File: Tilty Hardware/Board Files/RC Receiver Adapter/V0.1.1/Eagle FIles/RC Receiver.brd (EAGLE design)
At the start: 38.1 x 50.8 mm, 27 parts, among them U1 ATMEGA328P, U2 LM2931, U3 AP7313SOT23R, U4 C74HC407514-SOIC, Y1 16MHz

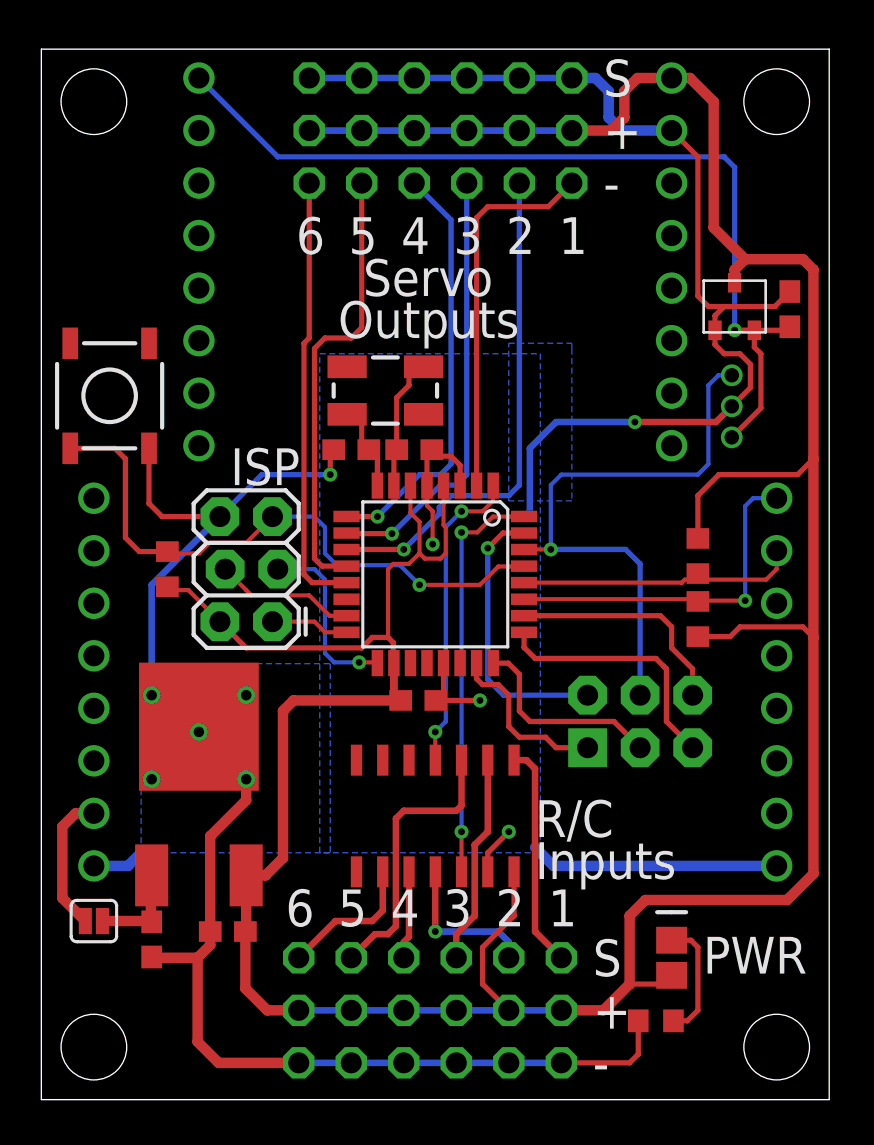
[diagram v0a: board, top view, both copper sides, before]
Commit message: R/C Receiver add-on work
fixed OR gate, moved reset button, corrected servo labels
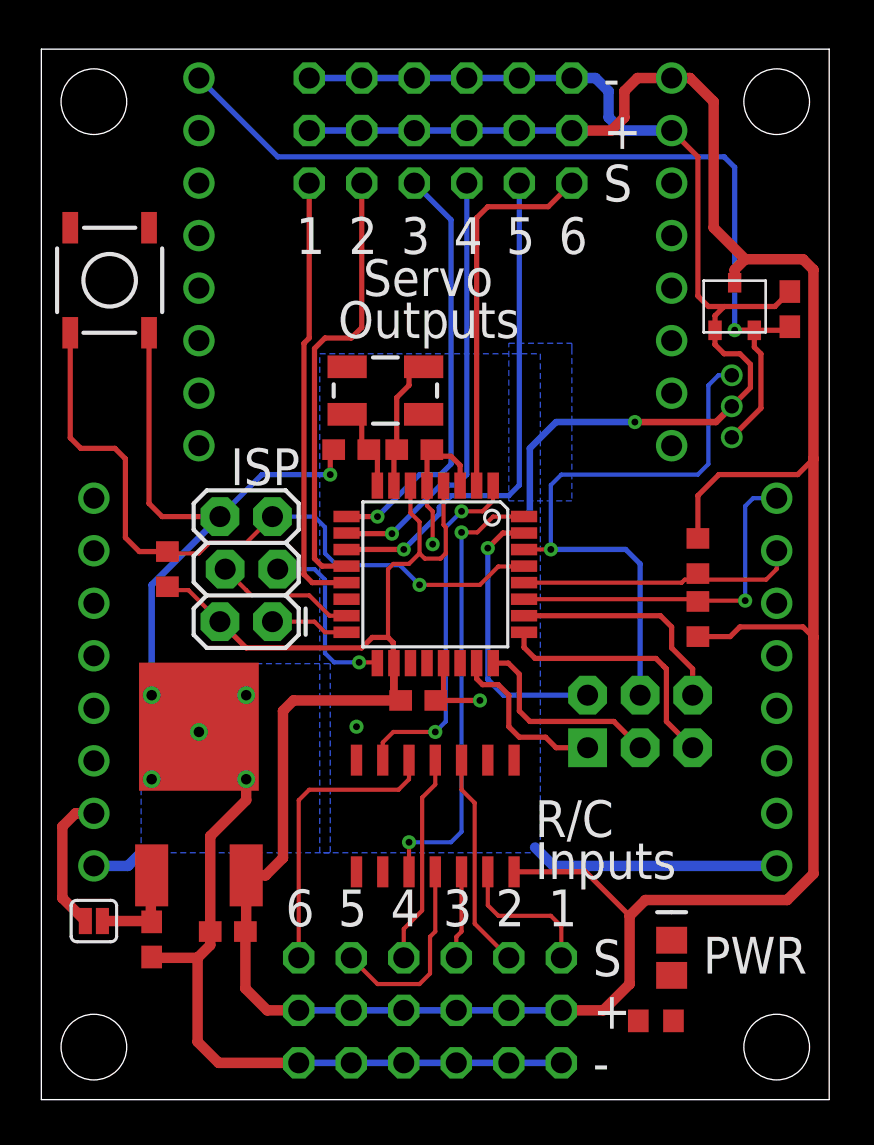
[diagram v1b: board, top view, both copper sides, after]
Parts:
- moved S1 5.59 mm to (3.30, 39.6)
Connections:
- net EVEN_CHAN: now also U1.1, U4.P$6; no longer U1.32, U4.P$12
- net GND: now also U4.P$7; no longer U4.P$13
- net ODD_CHAN: now also U1.32, U4.P$10; no longer U1.1, U4.P$4
- net SIGNAL_1: now also U4.P$13; no longer U4.P$1
- net SIGNAL_2: now also U4.P$3; no longer U4.P$11
- net SIGNAL_3: now also U4.P$12; no longer U4.P$2
- net SIGNAL_4: now also U4.P$4; no longer U4.P$10
- net SIGNAL_5: now also U4.P$11; no longer U4.P$3
- net SIGNAL_6: now also U4.P$5; no longer U4.P$9
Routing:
- net SIGNAL_6: track 6.88 -> 14.3 mm
- net ODD_CHAN: track 15.0 -> 22.0 mm
- net SIGNAL_4: track 4.26 -> 10.2 mm
- net SIGNAL_3: track 10.2 -> 4.26 mm
- net N$8: track 5.85 -> 0.00 mm
- net RESET: track 29.6 -> 34.9 mm
- net SIGNAL_5: track 13.6 -> 9.57 mm
- net SIGNAL_1: track 10.9 -> 7.12 mm
- net +5V: track 170.6 -> 167.0 mm
- net SIGNAL_2: track 7.42 -> 10.5 mm, vias 1 -> 0
- net EVEN_CHAN: track 19.8 -> 17.3 mm
- net GND: track 145.0 -> 142.7 mm

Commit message: RC Receiver add-on tweaking, updating things.todo handling
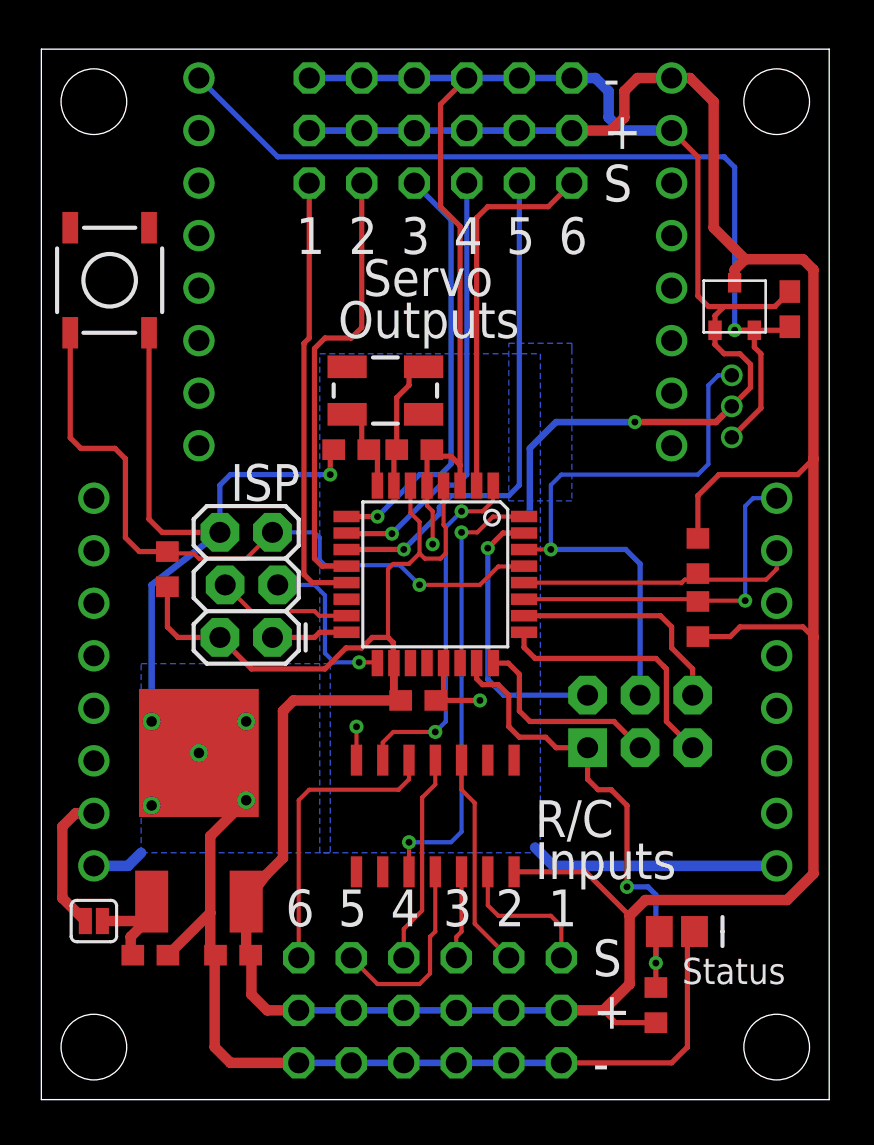
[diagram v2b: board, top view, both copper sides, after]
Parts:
- moved D1 1.30 mm to (30.7, 8.13), turned to 0 degrees
- moved U2 1.27 mm to (7.62, 14.0)
- moved C6 1.17 mm to (9.27, 6.99)
- moved C7 0.76 mm to (5.27, 6.99), turned to 0 degrees
- moved JP6 0.76 mm to (11.2, 22.4)
- moved R4 0.76 mm to (29.7, 4.57), turned to 270 degrees
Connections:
- removed net A0: JP10.1, U1.23
- removed net N$8: D1.2, R4.2
- new net STATUS_LED: D1.1, JP10.1, R4.1, U1.23
- net +5V: now also R4.2; no longer D1.1
- net GND: now also D1.2; no longer R4.1
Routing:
- net GND: track 142.7 -> 177.9 mm
- net STATUS_LED: track 0.00 -> 23.9 mm, vias 0 -> 2
- net A0: track 8.40 -> 0.00 mm
- net +5V: track 167.0 -> 171.3 mm
- net +24V: track 4.62 -> 7.75 mm
- net SCK: track 8.79 -> 8.02 mm
- net RESET: track 34.9 -> 34.3 mm
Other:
- board text added: "Status"
- board text removed: "PWR"

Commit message: Made final revisions to Tilty Omni and R/C Receiver adapter before ordering!
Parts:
- added D2: (no value), SparkFun-LED:LED-0805
- added R5: 220, resistor:R0603
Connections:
- new net N$4: D2.1, R5.1
- net +5V: now also R5.2
- net GND: now also D2.2
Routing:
- net +5V: track 171.3 -> 182.2 mm, vias 0 -> 1
- net N$4: track 0.00 -> 9.90 mm
- net GND: track 177.9 -> 178.4 mm
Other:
- board text added: "3v3"
- board text added: "5v"
- board text added: "GND"
- board text added: "ICSP"
- board text added: "PWR"
- board text added: "Reset"
- board text removed: "ISP"
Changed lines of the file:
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@@
 <setting verticaltext="up"/>
 </settings>
-<grid distance="0.01" unitdist="inch" unit="inch" style="lines" multiple="1" display="yes" altdistance="0.0025" altunitdist="inch" altunit="inch"/>
+<grid distance="500" unitdist="inch" unit="inch" style="lines" multiple="1" display="yes" altdistance="0.0025" altunitdist="inch" altunit="inch"/>
 <layers>
 <layer number="1" name="Top" color="4" fill="1" visible="yes" active="yes"/>
@@
 <text x="29.845" y="24.638" size="1.778" layer="26" ratio="12" rot="MR270">RX</text>
 <text x="27.305" y="24.638" size="1.778" layer="26" ratio="12" rot="MR270">TX</text>
-<text x="9.144" y="28.956" size="1.778" layer="25" ratio="12">ISP</text>
+<text x="9.0805" y="28.956" size="1.778" layer="25" ratio="12">ICSP</text>
 <wire x1="24.638" y1="11.684" x2="24.638" y2="24.892" width="0.635" layer="26"/>
 <wire x1="24.638" y1="24.892" x2="33.274" y2="24.892" width="0.635" layer="26"/>
@@
 <text x="31.496" y="26.924" size="1.27" layer="26" ratio="15" rot="MR0">Extra</text>
 <text x="30.988" y="25.4" size="1.27" layer="26" ratio="15" rot="MR0">Pins</text>
+<text x="6.096" y="3.556" size="1.778" layer="25" ratio="15">PWR</text>
+<text x="0.635" y="34.544" size="1.27" layer="25" ratio="15">Reset</text>
+<text x="29.21" y="48.768" size="1.27" layer="26" ratio="15" rot="MR0">5v</text>
+<text x="34.036" y="44.196" size="1.27" layer="26" ratio="15" rot="MR30">GND</text>
+<text x="11.938" y="48.768" size="1.27" layer="26" ratio="15" rot="MR0">3v3</text>
 </plain>
 <attributes>
@@
 </element>
 <element name="S1" library="SparkFun-Electromechanical" package="TACTILE_SWITCH_SMD" value="SWITCH-MOMENTARY-2SMD" x="3.302" y="39.624" smashed="yes" rot="R90"/>
+<element name="D2" library="SparkFun-LED" package="LED-0805" value="" x="7.874" y="2.032" smashed="yes">
+<attribute name="VALUE" x="7.112" y="-0.889" size="1.27" layer="27"/>
+</element>
+<element name="R5" library="resistor" package="R0603" value="220" x="2.2225" y="6.985" smashed="yes"/>
 </elements>
 <signals>
@@
 <wire x1="8.167" y1="12.739" x2="9.906" y2="14.478" width="0.508" layer="1"/>
 <via x="7.62" y="16.764" extent="1-16" drill="0.508"/>
-<via x="13.97" y="30.226" extent="1-16" drill="0.3302"/>
-<wire x1="13.97" y1="30.226" x2="13.97" y2="31.2665" width="0.254" layer="1"/>
-<wire x1="13.97" y1="31.2665" x2="14.136" y2="31.4325" width="0.254" layer="1"/>
-<wire x1="9.144" y1="30.226" x2="13.97" y2="30.226" width="0.254" layer="16"/>
+<via x="14.9225" y="29.337" extent="1-16" drill="0.3302"/>
 <polygon width="0.254" layer="16">
 <vertex x="13.97" y="11.938"/>
@@
 <wire x1="8.167" y1="9.0315" x2="8.167" y2="7.239" width="0.508" layer="1"/>
 <wire x1="8.167" y1="7.239" x2="8.421" y2="6.985" width="0.508" layer="1"/>
-<wire x1="12.446" y1="1.778" x2="9.144" y2="1.778" width="0.508" layer="1"/>
-<wire x1="9.144" y1="1.778" x2="8.382" y2="2.54" width="0.508" layer="1"/>
-<wire x1="8.382" y1="2.54" x2="8.382" y2="6.946" width="0.508" layer="1"/>
 <wire x1="8.382" y1="6.946" x2="8.421" y2="6.985" width="0.508" layer="1"/>
 <wire x1="5.207" y1="28.067" x2="5.842" y2="27.432" width="0.254" layer="1"/>
 <wire x1="5.842" y1="27.432" x2="8.636" y2="27.432" width="0.254" layer="1"/>
-<wire x1="9.144" y1="30.226" x2="8.636" y2="29.718" width="0.254" layer="16"/>
-<wire x1="8.636" y1="29.718" x2="8.636" y2="27.432" width="0.254" layer="16"/>
 <wire x1="15.24" y1="16.416" x2="15.24" y2="18.034" width="0.2032" layer="1"/>
 <wire x1="20.25" y1="30.677" x2="20.25" y2="42.234" width="0.254" layer="1"/>
@@
 <wire x1="19.304" y1="43.18" x2="19.304" y2="48.133" width="0.254" layer="1"/>
 <wire x1="19.304" y1="48.133" x2="20.574" y2="49.403" width="0.254" layer="1"/>
+<contactref element="D2" pad="2"/>
+<wire x1="12.446" y1="1.778" x2="8.978" y2="1.778" width="0.508" layer="1"/>
+<wire x1="8.978" y1="1.778" x2="8.724" y2="2.032" width="0.508" layer="1"/>
+<wire x1="8.724" y1="2.032" x2="8.724" y2="6.682" width="0.508" layer="1"/>
+<wire x1="8.724" y1="6.682" x2="8.421" y2="6.985" width="0.508" layer="1"/>
+<wire x1="14.136" y1="31.4325" x2="14.136" y2="30.1235" width="0.254" layer="1"/>
+<wire x1="14.136" y1="30.1235" x2="14.9225" y2="29.337" width="0.254" layer="1"/>
+<wire x1="14.9225" y1="29.337" x2="10.541" y2="29.337" width="0.254" layer="16"/>
+<wire x1="10.541" y1="29.337" x2="8.636" y2="27.432" width="0.254" layer="16"/>
 </signal>
 <signal name="+24V">
@@
 <wire x1="6.604" y1="22.352" x2="6.096" y2="22.86" width="0.254" layer="1"/>
 <wire x1="6.096" y1="22.86" x2="6.096" y2="24.804" width="0.254" layer="1"/>
+<contactref element="R5" pad="2"/>
+<via x="7.239" y="6.0325" extent="1-16" drill="0.3302"/>
+<wire x1="3.0725" y1="6.985" x2="3.0725" y2="6.389" width="0.2032" layer="1"/>
+<wire x1="3.0725" y1="6.389" x2="3.429" y2="6.0325" width="0.2032" layer="1"/>
+<wire x1="3.429" y1="6.0325" x2="7.239" y2="6.0325" width="0.2032" layer="1"/>
+<wire x1="7.239" y1="6.0325" x2="10.7315" y2="6.0325" width="0.2032" layer="16"/>
+<wire x1="10.7315" y1="6.0325" x2="12.446" y2="4.318" width="0.2032" layer="16"/>
 </signal>
 <signal name="N$5">
@@
 <wire x1="21.05" y1="20.352" x2="21.05" y2="21.1074" width="0.254" layer="1"/>
 </signal>
+<signal name="N$4">
+<contactref element="D2" pad="1"/>
+<contactref element="R5" pad="1"/>
+<wire x1="1.3725" y1="6.985" x2="1.3725" y2="5.4855" width="0.2032" layer="1"/>
+<wire x1="1.3725" y1="5.4855" x2="2.032" y2="4.826" width="0.2032" layer="1"/>
+<wire x1="2.032" y1="4.826" x2="6.477" y2="4.826" width="0.2032" layer="1"/>
+<wire x1="6.477" y1="4.826" x2="6.985" y2="4.318" width="0.2032" layer="1"/>
+<wire x1="6.985" y1="4.318" x2="6.985" y2="2.071" width="0.2032" layer="1"/>
+<wire x1="6.985" y1="2.071" x2="7.024" y2="2.032" width="0.2032" layer="1"/>
+</signal>
 </signals>

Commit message: Lots of little updates!
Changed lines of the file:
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@@
 <setting verticaltext="up"/>
 </settings>
-<grid distance="500" unitdist="inch" unit="inch" style="lines" multiple="1" display="yes" altdistance="0.0025" altunitdist="inch" altunit="inch"/>
+<grid distance="0.01" unitdist="inch" unit="inch" style="lines" multiple="1" display="yes" altdistance="0.0025" altunitdist="inch" altunit="inch"/>
 <layers>
 <layer number="1" name="Top" color="4" fill="1" visible="yes" active="yes"/>
@@
 <text x="34.036" y="44.196" size="1.27" layer="26" ratio="15" rot="MR30">GND</text>
 <text x="11.938" y="48.768" size="1.27" layer="26" ratio="15" rot="MR0">3v3</text>
+<text x="25.527" y="24.638" size="1.778" layer="25" ratio="12" rot="R270">TX</text>
+<text x="28.067" y="24.638" size="1.778" layer="25" ratio="12" rot="R270">RX</text>
 </plain>
 <attributes>
@@
 <contactref element="R2" pad="1"/>
 <via x="34.036" y="24.13" extent="1-16" drill="0.3302"/>
-<wire x1="35.56" y1="29.083" x2="34.417" y2="29.083" width="0.2032" layer="16"/>
-<wire x1="34.417" y1="29.083" x2="34.036" y2="28.702" width="0.2032" layer="16"/>
-<wire x1="34.036" y1="28.702" x2="34.036" y2="24.13" width="0.2032" layer="16"/>
-<wire x1="34.036" y1="24.13" x2="31.789" y2="24.13" width="0.2032" layer="1"/>
 <wire x1="31.789" y1="24.13" x2="31.75" y2="24.091" width="0.2032" layer="1"/>
-<wire x1="23.3426" y1="24.2" x2="31.641" y2="24.2" width="0.2032" layer="1"/>
 <wire x1="31.641" y1="24.2" x2="31.75" y2="24.091" width="0.2032" layer="1"/>
+<wire x1="35.56" y1="29.083" x2="34.417" y2="29.083" width="0.1524" layer="16"/>
+<wire x1="34.417" y1="29.083" x2="34.036" y2="28.702" width="0.1524" layer="16"/>
+<wire x1="34.036" y1="28.702" x2="34.036" y2="24.13" width="0.1524" layer="16"/>
+<wire x1="34.036" y1="24.13" x2="31.789" y2="24.13" width="0.1524" layer="1"/>
+<wire x1="23.3426" y1="24.2" x2="31.641" y2="24.2" width="0.1524" layer="1"/>
 </signal>
 <signal name="SCL">
@@
 <contactref element="U1" pad="28"/>
 <contactref element="R3" pad="1"/>
-<wire x1="35.56" y1="26.543" x2="35.56" y2="25.654" width="0.2032" layer="1"/>
-<wire x1="35.56" y1="25.654" x2="35.052" y2="25.146" width="0.2032" layer="1"/>
-<wire x1="35.052" y1="25.146" x2="32.043" y2="25.146" width="0.2032" layer="1"/>
 <wire x1="32.043" y1="25.146" x2="31.75" y2="25.439" width="0.2032" layer="1"/>
-<wire x1="23.3426" y1="25" x2="30.969" y2="25" width="0.2032" layer="1"/>
-<wire x1="30.969" y1="25" x2="31.115" y2="25.146" width="0.2032" layer="1"/>
-<wire x1="31.115" y1="25.146" x2="31.457" y2="25.146" width="0.2032" layer="1"/>
-<wire x1="31.457" y1="25.146" x2="31.75" y2="25.439" width="0.2032" layer="1"/>
+<wire x1="32.043" y1="25.146" x2="23.4886" y2="25.146" width="0.1524" layer="1"/>
+<wire x1="23.4886" y1="25.146" x2="23.3426" y2="25" width="0.1524" layer="1"/>
+<wire x1="32.043" y1="25.146" x2="34.163" y2="25.146" width="0.1524" layer="1"/>
+<wire x1="34.163" y1="25.146" x2="35.56" y2="26.543" width="0.1524" layer="1"/>
 </signal>
 <signal name="SIGNAL_1">
@@
 <wire x1="32.258" y1="34.544" x2="32.258" y2="30.734" width="0.2032" layer="16"/>
 <contactref element="JP10" pad="4"/>
-<wire x1="24.638" y1="26.6065" x2="28.2575" y2="26.6065" width="0.254" layer="16"/>
-<wire x1="28.2575" y1="26.6065" x2="28.956" y2="25.908" width="0.254" layer="16"/>
-<wire x1="28.956" y1="25.908" x2="28.956" y2="19.558" width="0.254" layer="16"/>
+<wire x1="24.638" y1="26.6065" x2="28.2575" y2="26.6065" width="0.1524" layer="16"/>
+<wire x1="28.2575" y1="26.6065" x2="28.956" y2="25.908" width="0.1524" layer="16"/>
+<wire x1="28.956" y1="25.908" x2="28.956" y2="19.558" width="0.1524" layer="16"/>
 </signal>
 <signal name="+3V3">
